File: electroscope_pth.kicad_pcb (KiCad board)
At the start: 2 copper layers, 17 parts, among them Q1 Q_PNP_EBC, Q2 Q_NPN_EBC, Q3 Q_PNP_EBC, Q4 Q_NPN_EBC, Q5 Q_PNP_EBC, Q6 Q_NPN_EBC, U1 ANT, U2 ANT

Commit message: Ready to mill
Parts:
- BT1: footprint electroscope_pth:BSPCMF-9VBATT-SNAP -> 9VBATT_TH:9VBATT_TH
- moved R6 30.4 mm to (142.2, 102.7)
- moved R1 30.3 mm to (136.1, 102.7)
- moved D2 30.3 mm to (142.2, 111.0)
- moved D1 30.1 mm to (136.1, 111.1)
- moved Q1 29.8 mm to (128.0, 101.3)
- moved Q4 29.7 mm to (150.2, 90.9)
- moved Q3 29.6 mm to (128.0, 90.9)
- moved Q2 29.5 mm to (150.2, 79.9)
- moved Q6 29.5 mm to (150.2, 101.3)
- moved BT1 29.4 mm to (138.9, 116.0)
- moved U1 29.1 mm to (142.2, 71.4)
- moved R3 29.0 mm to (136.3, 91.6)
- moved R2 28.8 mm to (142.2, 81.1), turned to 90 degrees
- moved R4 28.8 mm to (142.2, 91.6), turned to 90 degrees
- moved R5 28.6 mm to (136.6, 81.3)
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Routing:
- net VCC: track 0.00 -> 71.5 mm
- net GND: track 0.00 -> 71.5 mm
- net Net-(Q5-Pad2): track 0.00 -> 23.9 mm
- net Net-(Q2-Pad2): track 0.00 -> 20.6 mm
- net Net-(D2-Pad2): track 0.00 -> 18.2 mm
- net Net-(Q2-Pad3): track 0.00 -> 11.0 mm
- net Net-(Q4-Pad3): track 0.00 -> 10.6 mm
- net Net-(Q2-Pad1): track 0.00 -> 8.45 mm
- net Net-(Q3-Pad2): track 0.00 -> 8.26 mm
- net Net-(Q4-Pad1): track 0.00 -> 7.87 mm
- net Net-(Q1-Pad2): track 0.00 -> 7.87 mm
- net Net-(Q5-Pad3): track 0.00 -> 7.32 mm
- net Net-(Q3-Pad3): track 0.00 -> 7.24 mm
- net Net-(Q1-Pad3): track 0.00 -> 6.89 mm
- net Net-(D1-Pad1): track 0.00 -> 4.61 mm
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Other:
- board outline added: 33 x 50.8 mm
- net class Default: clearance 0.2 -> 0.39878; trace_width 0.25 -> 0.508
- rule trace_clearance: 0.2 -> 0.39878
- rule trace_min: 0.2 -> 0.2032

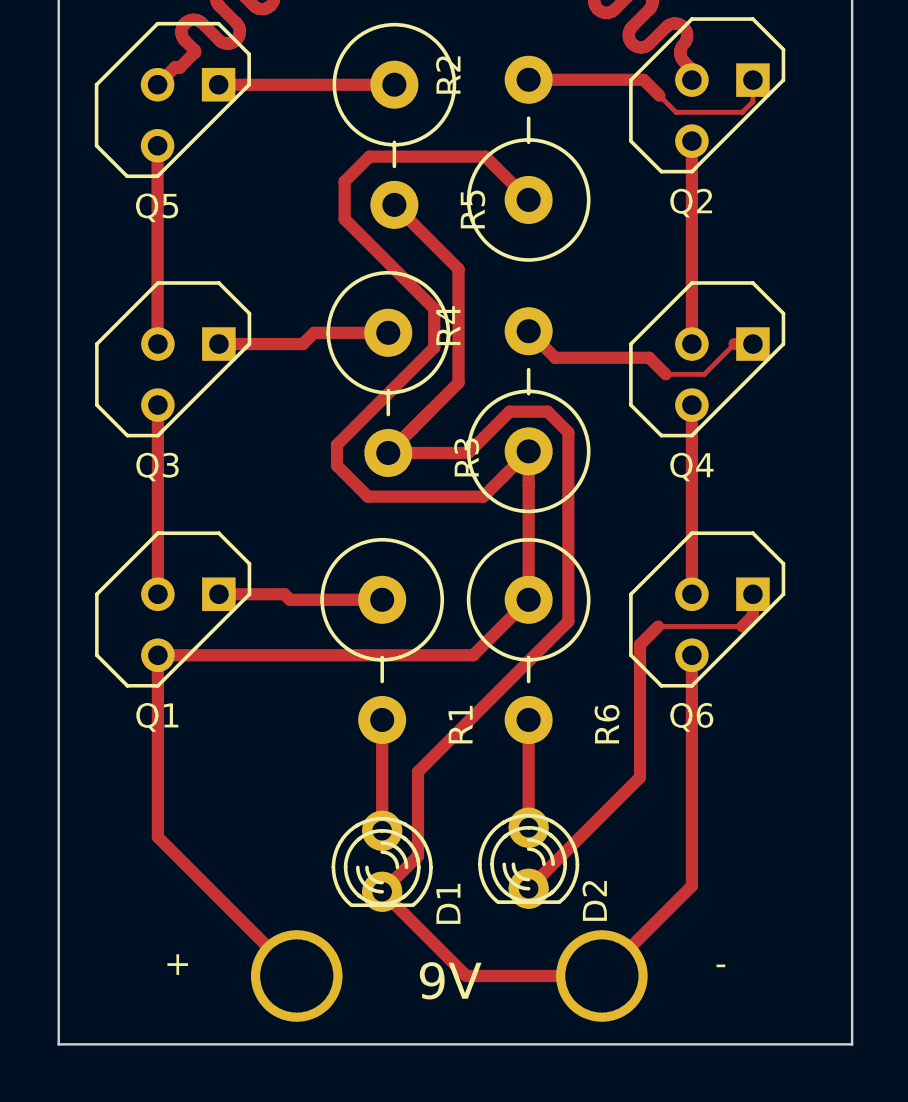
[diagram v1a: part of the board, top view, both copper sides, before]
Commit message: Add isolated plane @ bottom 3/4ths or so of board
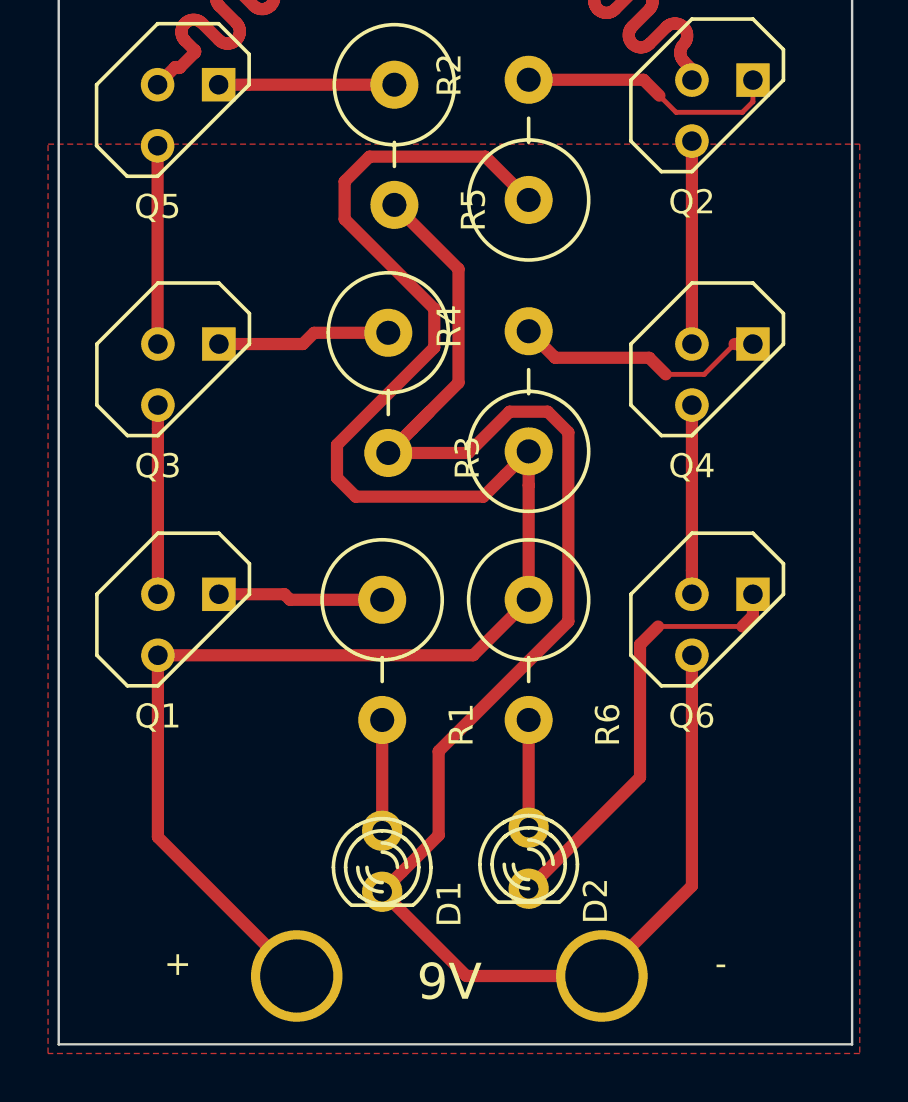
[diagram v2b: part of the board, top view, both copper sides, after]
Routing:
- added copper zone on F.Cu, net (none)
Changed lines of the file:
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@@
     (links 22)
     (no_connects 0)
-    (area 122.568499 67.894999 155.688501 118.795001)
+    (area 121.997615 66.93872 155.688501 118.795001)
     (thickness 1.6)
     (drawings 4)
@@
     (user_trace_width 0.2032)
     (trace_clearance 0.39878)
-    (zone_clearance 0.508)
+    (zone_clearance 1.016)
     (zone_45_only no)
     (trace_min 0.2032)
@@
     (visible_elements FFFFFF7F)
     (pcbplotparams
-      (layerselection 0x00030_80000001)
+      (layerselection 0x010f0_80000001)
       (usegerberextensions false)
       (excludeedgelayer true)
@@
       (outputformat 1)
       (mirror false)
-      (drillshape 1)
+      (drillshape 0)
       (scaleselection 1)
-      (outputdirectory ""))
+      (outputdirectory gerbers/))
   )
   (net 0 "")
@@
   (segment (start 140.374369 81.799429) (end 135.551061 81.799429) (width 0.508) (layer F.Cu) (net 1))
   (segment (start 135.551061 81.799429) (end 134.517129 82.833361) (width 0.508) (layer F.Cu) (net 1))
-  (segment (start 135.487561 95.949771) (end 140.293089 95.949771) (width 0.508) (layer F.Cu) (net 1))
+  (segment (start 134.979561 95.949771) (end 140.293089 95.949771) (width 0.508) (layer F.Cu) (net 1))
   (segment (start 134.517129 82.833361) (end 134.517129 84.400239) (width 0.508) (layer F.Cu) (net 1))
   (segment (start 134.517129 84.400239) (end 138.248381 88.131491) (width 0.508) (layer F.Cu) (net 1))
@@
   (segment (start 138.248381 89.744709) (end 134.199629 93.793461) (width 0.508) (layer F.Cu) (net 1))
   (segment (start 140.293089 95.949771) (end 141.177011 95.065849) (width 0.508) (layer F.Cu) (net 1))
-  (segment (start 134.199629 93.793461) (end 134.199629 94.661839) (width 0.508) (layer F.Cu) (net 1))
-  (segment (start 134.199629 94.661839) (end 135.487561 95.949771) (width 0.508) (layer F.Cu) (net 1))
+  (segment (start 134.199629 93.793461) (end 134.199629 95.169839) (width 0.508) (layer F.Cu) (net 1))
+  (segment (start 134.199629 95.169839) (end 134.979561 95.949771) (width 0.508) (layer F.Cu) (net 1))
   (segment (start 142.1765 94.06636) (end 142.1765 95.479852) (width 0.508) (layer F.Cu) (net 1))
   (segment (start 142.1765 95.479852) (end 142.1765 100.24364) (width 0.508) (layer F.Cu) (net 1))
@@
   (segment (start 136.3345 94.1324) (end 138.052811 92.414089) (width 0.508) (layer F.Cu) (net 2))
   (segment (start 142.969591 92.414089) (end 143.828771 93.273269) (width 0.508) (layer F.Cu) (net 2))
-  (segment (start 137.571481 107.404557) (end 137.571481 110.904019) (width 0.508) (layer F.Cu) (net 2))
+  (segment (start 138.43 106.546038) (end 138.43 110.0455) (width 0.508) (layer F.Cu) (net 2))
   (segment (start 143.828771 93.273269) (end 143.828771 101.147267) (width 0.508) (layer F.Cu) (net 2))
-  (segment (start 143.828771 101.147267) (end 137.571481 107.404557) (width 0.508) (layer F.Cu) (net 2))
-  (segment (start 137.571481 110.904019) (end 136.918699 111.556801) (width 0.508) (layer F.Cu) (net 2))
+  (segment (start 143.828771 101.147267) (end 138.43 106.546038) (width 0.508) (layer F.Cu) (net 2))
+  (segment (start 138.43 110.0455) (end 136.918699 111.556801) (width 0.508) (layer F.Cu) (net 2))
   (segment (start 136.918699 111.556801) (end 136.0805 112.395) (width 0.508) (layer F.Cu) (net 2))
   (segment (start 136.5885 83.8073) (end 139.256771 86.475571) (width 0.508) (layer F.Cu) (net 2))
@@
   (segment (start 148.971 100.0125) (end 148.971 99.024672) (width 0.508) (layer F.Cu) (net 16))
   (segment (start 148.971 99.024672) (end 148.971 92.1385) (width 0.508) (layer F.Cu) (net 16))
+  (zone (net 0) (net_name "") (layer F.Cu) (hatch edge 0.508)
+    (connect_pads (clearance 1.016))
+    (min_thickness 0.254)
+    (fill yes (arc_segments 32) (thermal_gap 0.508) (thermal_bridge_width 0.508))
+    (polygon
+      (pts
+        (xy 155.956 119.126) (xy 122.174 119.126) (xy 122.174 81.28) (xy 155.956 81.28)
+      )
+    )
+  )
 )

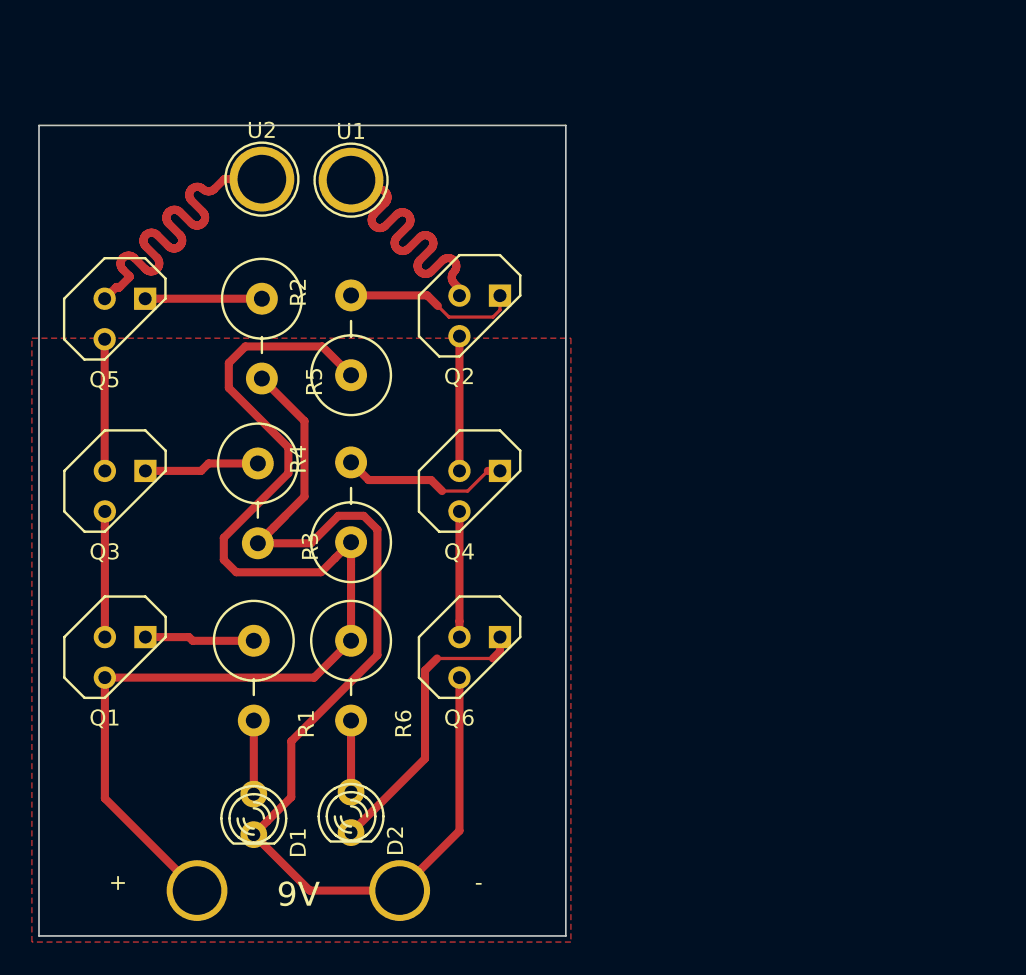
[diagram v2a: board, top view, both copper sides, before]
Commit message: Re-route PCB with centered dimensions and rework footprint silkscreens
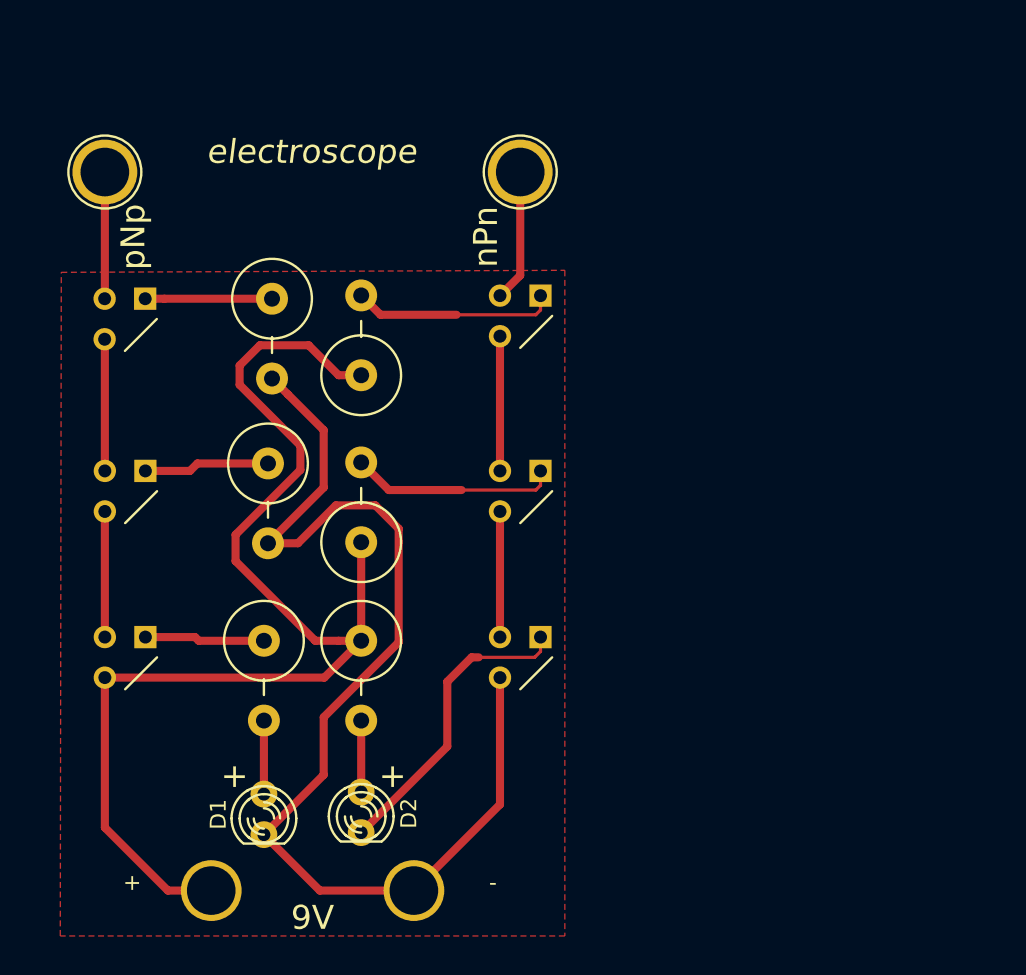
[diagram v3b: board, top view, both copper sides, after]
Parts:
- Q1, Q2, Q3, Q4, Q5, Q6: footprint Discret:TO92-123 -> transistors:TO92-123
- moved U1 10.6 mm to (152.8, 70.9)
- moved U2 9.85 mm to (126.7, 70.9)
- moved Q2 2.54 mm to (152.8, 79.9)
- moved Q4 2.54 mm to (152.8, 90.9)
- moved Q6 2.54 mm to (152.8, 101.3)
- moved BT1 0.89 mm to (139.8, 116.0)
- moved D1 0.63 mm to (136.7, 111.1)
- moved D2 0.63 mm to (142.8, 111.0)
- moved R1 0.63 mm to (136.7, 102.7)
- moved R2 0.63 mm to (142.8, 81.1)
- moved R3 0.63 mm to (137.0, 91.6)
- moved R4 0.63 mm to (142.8, 91.6)
- moved R5 0.63 mm to (137.2, 81.3)
- moved R6 0.63 mm to (142.8, 102.7)
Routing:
- net Net-(Q5-Pad2): track 23.9 -> 7.95 mm
- net Net-(Q2-Pad2): track 20.6 -> 8.27 mm
- net VCC: track 71.8 -> 75.3 mm
- net Net-(Q4-Pad3): track 10.6 -> 13.0 mm
- net Net-(Q2-Pad3): track 11.0 -> 12.8 mm
- net Net-(D2-Pad2): track 18.2 -> 19.2 mm
- net Net-(Q5-Pad3): track 7.32 -> 7.95 mm
- net Net-(Q3-Pad3): track 7.24 -> 7.88 mm
- net Net-(Q1-Pad3): track 6.89 -> 7.52 mm
- net GND: track 71.5 -> 72.0 mm
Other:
- board outline removed
- board text added: "+"
- board text added: "electroscope"
- board text added: "nPn"
- board text added: "pNp"
